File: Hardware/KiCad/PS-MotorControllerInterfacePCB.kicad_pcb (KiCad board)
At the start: 2 copper layers, 59.1 x 75.7 mm, 118 parts, among them IC1 LM74502HDDFR, IC2 LM74502HDDFR, J1 CAN board out, J2 PWR board, J3 CAN board in, J4 53307-2471, J5 PWR Moco, J6 Candapter, J7 CAN board -> mppt +moco, J8 CAN mppts + moco -> board, J9 Conn_01x06, Q1 IRLML0030, Q2 IRLML0030, Q3 NVMFWS1D7N04XMT1G, Q4 NVMFWS1D7N04XMT1G, Q5 771-BUK6M61-60PX, Q6 NVMFWS1D7N04XMT1G, Q7 NVMFWS1D7N04XMT1G, U1 LMR33630ADDA

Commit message: revb
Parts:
- moved 12V1 6.72 mm to (198.9, 70.3), turned to 0 degrees
- moved R3 5.44 mm to (198.9, 68.4), turned to 0 degrees
- moved Q1 5.19 mm to (194.3, 96.3)
- moved R_PD1 5.19 mm to (194.4, 93.5)
- moved R_G1 5.18 mm to (194.4, 91.9)
- moved TP6 5.16 mm to (190.4, 96.1)
- moved LED6 5.15 mm to (190.4, 94.2), turned to 0 degrees
- moved R25 5.15 mm to (190.4, 92.6), turned to 180 degrees
- moved TP7 3.76 mm to (185.2, 96.1)
- moved LED7 3.74 mm to (185.2, 94.2), turned to 0 degrees
- moved R26 3.74 mm to (185.2, 92.7), turned to 180 degrees
- moved LVPWR2 3.33 mm to (198.9, 66.8), turned to 180 degrees
- moved LED5 2.47 mm to (179.9, 94.2)
- moved R24 2.47 mm to (179.9, 92.7)
- moved TP5 2.42 mm to (180.0, 96.1)
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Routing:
- net GND: track 28.6 -> 44.1 mm, vias 8 -> 12
- net /PWM_FAN_A: track 55.2 -> 59.9 mm
- net /Fans/FAN_B_NEG: track 15.4 -> 19.2 mm
- net /LED4: track 13.9 -> 17.6 mm
- net /LED5: track 11.3 -> 13.6 mm
- net /LED3: track 7.47 -> 9.74 mm
- net /PWM_FAN_B: track 36.9 -> 38.9 mm
- net /FANS_IN: track 59.8 -> 61.2 mm
- net /LED1: track 11.8 -> 13.1 mm
- net /CAN_H: track 154.5 -> 155.6 mm
- net /CAN_L: track 145.2 -> 146.3 mm
- net Net-(LVPWR2-A): track 2.47 -> 1.66 mm
- net +24V: track 19.8 -> 20.5 mm
- net /LED2: track 8.11 -> 8.67 mm
- net /FAN_B_TACHO: track 34.1 -> 34.7 mm

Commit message: cleanup
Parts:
- moved LVPWR2 0.74 mm to (198.8, 67.5)
- moved R3 0.69 mm to (198.8, 69.1)
- moved 12V1 0.61 mm to (198.8, 70.9)
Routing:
- net GND: track 44.1 -> 44.5 mm, vias 12 -> 234
- added copper zone on B.Cu, net /12V_BUS
- added copper zone on B.Cu, net /VIN_24V

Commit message: sch changes, pre pcb changes
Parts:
- J1, J3: footprint Connector_Molex:Molex_Nano-Fit_105314-xx06_2x03_P2.50mm_Horizontal -> UTSVT_Connectors:105314-1306
- J2, J5, J6: footprint Connector_Molex:Molex_Nano-Fit_105313-xx02_1x02_P2.50mm_Horizontal -> UTSVT_Connectors:105313-2102
- J7, J8: footprint Connector_Molex:Molex_Nano-Fit_105313-xx03_1x03_P2.50mm_Horizontal -> UTSVT_Connectors:105313-1103
- J9: footprint Connector_Molex:Molex_Nano-Fit_105313-xx06_1x06_P2.50mm_Horizontal -> UTSVT_Connectors:105313-1106
- moved H3 57.8 mm to (157.8, 92.5)
- moved J7 10.3 mm to (202.5, 59.5), turned to 0 degrees
- moved J8 10.1 mm to (205.2, 47.9), turned to 90 degrees
- moved J2 9.24 mm to (198.1, 47.9), turned to 90 degrees
- moved J5 7.51 mm to (202.6, 70.3), turned to 0 degrees
- moved 3V1 6.02 mm to (155.1, 87.6)
- moved LVPWR3 6.02 mm to (155.0, 84.2)
- moved R5 6.02 mm to (155.0, 85.7)
- moved C2 2.81 mm to (178.7, 61.2), turned to -90 degrees
- moved R15 1.68 mm to (182.3, 86.0)
- moved Z3 1.46 mm to (182.8, 61.3)
- moved 12V1 1.18 mm to (198.0, 71.8)
- moved LVPWR2 1.15 mm to (197.9, 68.3)
- moved R3 1.11 mm to (198.0, 69.8)
- moved J4 0.99 mm to (176.4, 86.1)
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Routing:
- net GND: track 44.5 -> 33.8 mm, vias 234 -> 219
- net Net-(U1-SW): track 8.25 -> 0.00 mm
- net +3V3: track 38.4 -> 46.3 mm
- net /CAN_H: track 155.6 -> 152.9 mm
- net /PWM_FAN_B: track 38.9 -> 36.4 mm
- net /RPP_EN12: track 17.3 -> 15.6 mm
- net /CAN_L: track 146.3 -> 147.8 mm
- net /FAN_B_TACHO: track 34.7 -> 33.6 mm
- net /LED3: track 9.74 -> 8.82 mm
- net /MESSAGE: track 28.9 -> 29.5 mm
- net /D_C: track 34.3 -> 34.9 mm
- net /S_OC: track 25.5 -> 26.1 mm
- net /M_FAULT: track 40.3 -> 40.8 mm
- added copper zone on F.Cu, net Net-(U1-SW)

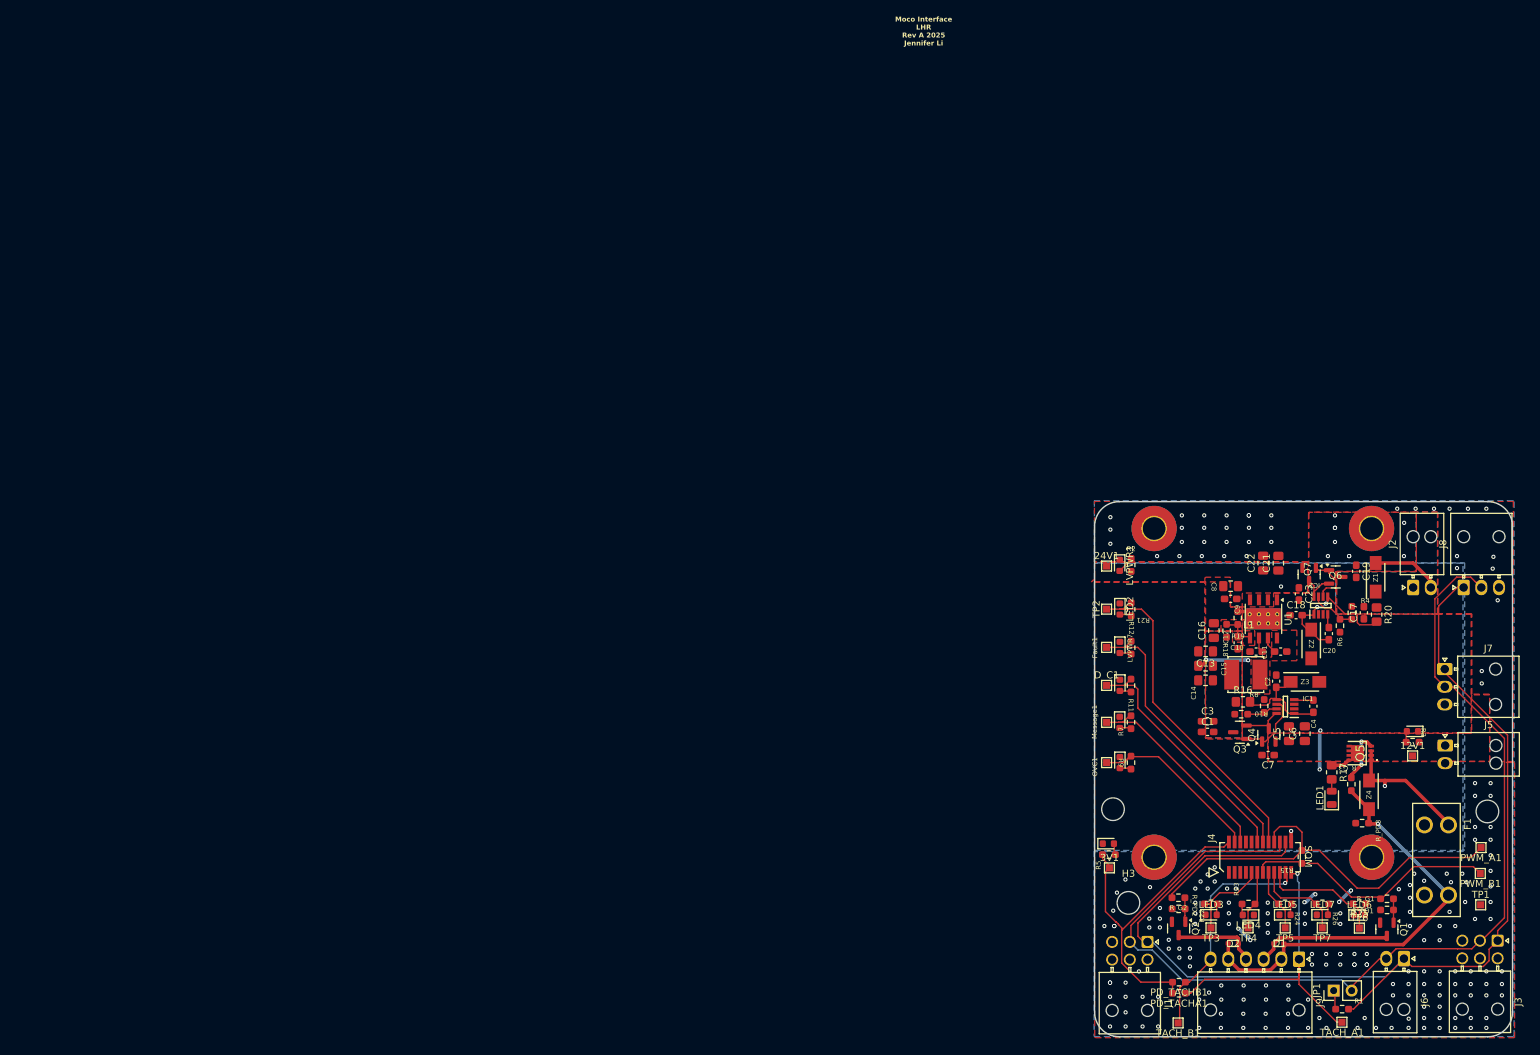
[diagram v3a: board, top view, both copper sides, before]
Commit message: layout ready for review
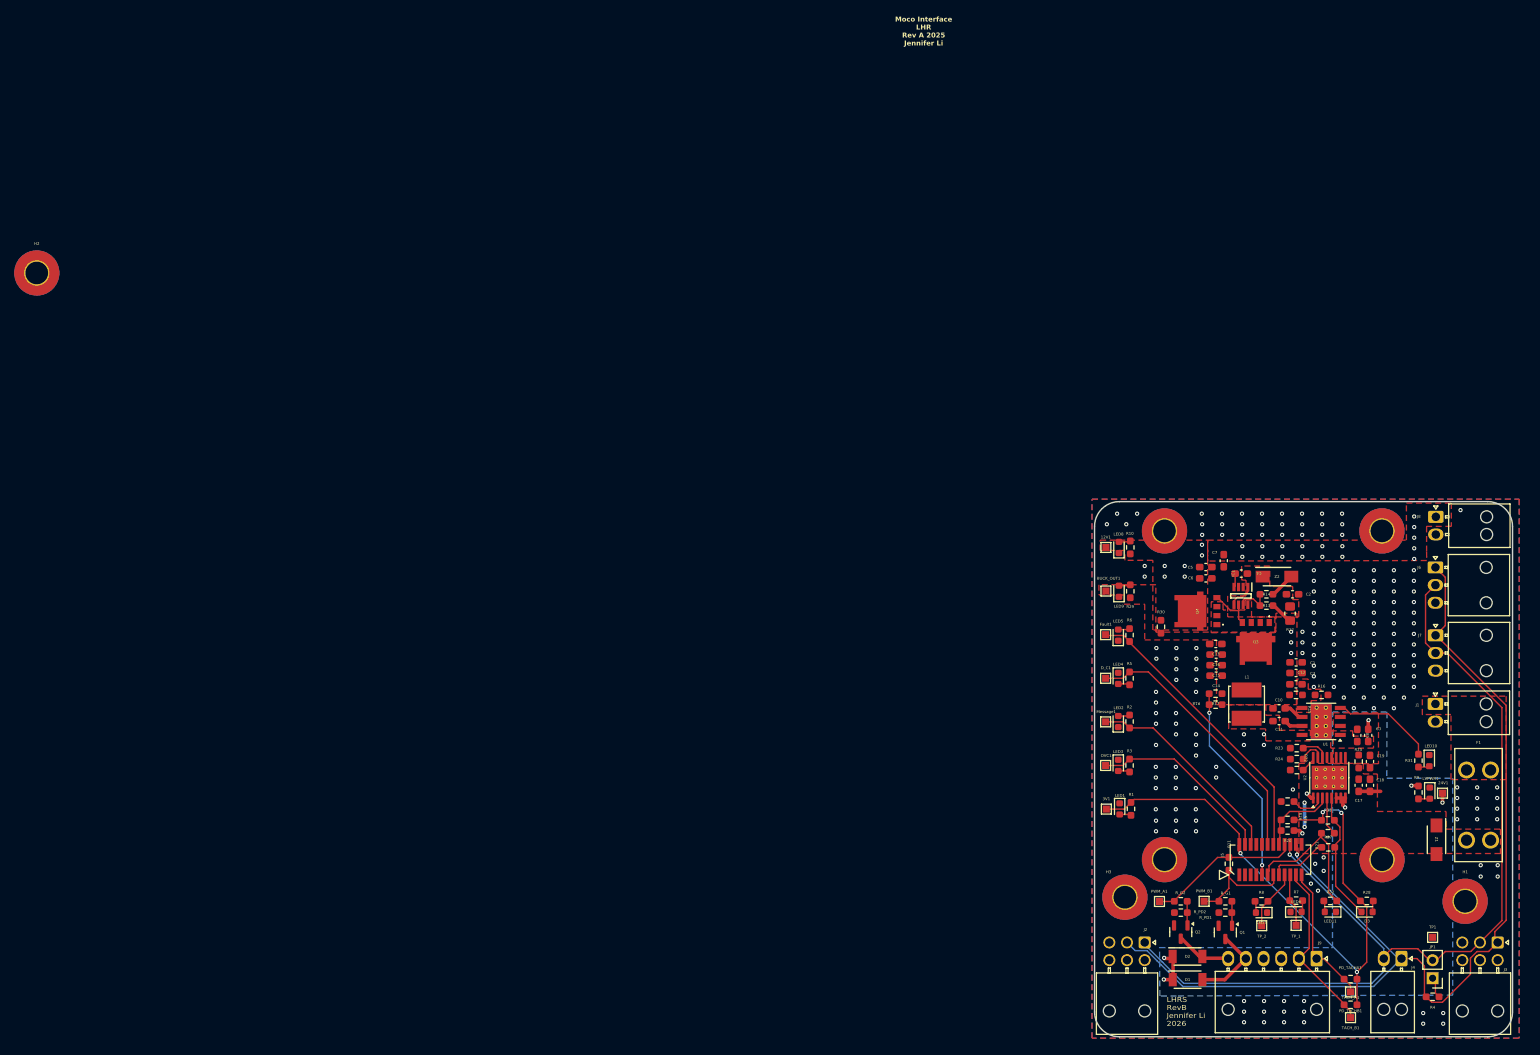
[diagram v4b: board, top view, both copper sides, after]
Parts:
- removed C20: 220n, Capacitor_SMD:C_0603_1608Metric_Pad1.08x0.95mm_HandSolder
- removed C21, C22: 10u, Capacitor_SMD:C_0805_2012Metric_Pad1.18x1.45mm_HandSolder
- removed C23: 0.1u, Capacitor_SMD:C_0603_1608Metric_Pad1.08x0.95mm_HandSolder
- removed IC2: LM74502HDDFR, UTSVT_Power:SOT65P280X110-8N
- removed LVPWR2, LVPWR3, LVPWR4, LVPWR5, LVPWR6, LVPWR7: LED, LED_SMD:LED_0603_1608Metric
- removed Q5: 771-BUK6M61-60PX, Moco:BUK9M34100EX
- removed Q6, Q7: NVMFWS1D7N04XMT1G, Package_TO_SOT_SMD:SOT-23
- removed R_G3: 100, Resistor_SMD:R_0603_1608Metric_Pad0.98x0.95mm_HandSolder
- removed R_PD3: 10k, Resistor_SMD:R_0603_1608Metric_Pad0.98x0.95mm_HandSolder
- removed TP2: LED, TestPoint:TestPoint_Pad_1.0x1.0mm
- removed TP3: LED1, TestPoint:TestPoint_Pad_1.0x1.0mm
- removed TP4: LED2, TestPoint:TestPoint_Pad_1.0x1.0mm
- removed TP5: LED3, TestPoint:TestPoint_Pad_1.0x1.0mm
- removed TP6: LED4, TestPoint:TestPoint_Pad_1.0x1.0mm
- removed TP7: LED5, TestPoint:TestPoint_Pad_1.0x1.0mm
- removed Z3: SMAF4758A, UTSVT_Passives:SODFL5026X125N
- removed Z4: SMAF4742A, UTSVT_Passives:SODFL5026X125N
- added BUCK_OUT1: TP_12V, TestPoint:TestPoint_Pad_1.0x1.0mm, F.Cu at (154.6, 48.4)
- added D3: LED_Small, LED_SMD:LED_0603_1608Metric, F.Cu at (191.5, 93.8)
- added LED10: LED, LED_SMD:LED_0603_1608Metric, F.Cu at (200.3, 72.4)
- added LED11: LED, LED_SMD:LED_0603_1608Metric, F.Cu at (186.3, 93.8)
- added LED8: LED, LED_SMD:LED_0603_1608Metric, F.Cu at (156.5, 42.3)
- added LED9: LED, LED_SMD:LED_0603_1608Metric, F.Cu at (156.5, 48.5)
- added R13: 100k, Resistor_SMD:R_0603_1608Metric_Pad0.98x0.95mm_HandSolder, F.Cu at (177.3, 50.5)
- added R14: 9。5k, Resistor_SMD:R_0603_1608Metric_Pad0.98x0.95mm_HandSolder, F.Cu at (177.3, 48.9)
- added R27: 10k, Resistor_SMD:R_0603_1608Metric_Pad0.98x0.95mm_HandSolder, F.Cu at (186.1, 84.7)
- added R28: 1k, Resistor_SMD:R_0603_1608Metric_Pad0.98x0.95mm_HandSolder, F.Cu at (191.5, 92.2)
- added R29: 4.3k, Resistor_SMD:R_0603_1608Metric_Pad0.98x0.95mm_HandSolder, F.Cu at (158.1, 48.5)
- added R30: 0, Resistor_SMD:R_0603_1608Metric_Pad0.98x0.95mm_HandSolder, F.Cu at (162.4, 53.5)
- added R31: 4.3k, Resistor_SMD:R_0603_1608Metric_Pad0.98x0.95mm_HandSolder, F.Cu at (198.8, 72.4)
- added R32: 1k, Resistor_SMD:R_0603_1608Metric_Pad0.98x0.95mm_HandSolder, F.Cu at (186.3, 92.2)
- added R33: 10k, Resistor_SMD:R_0603_1608Metric_Pad0.98x0.95mm_HandSolder, F.Cu at (186.0, 80.8)
- added TP_1: LED1, TestPoint:TestPoint_Pad_1.0x1.0mm, F.Cu at (181.5, 95.7)
- added TP_2: LED2, TestPoint:TestPoint_Pad_1.0x1.0mm, F.Cu at (176.6, 95.8)
- added U2: TPS27SA08-Q1, Package_SO:HTSSOP-16-1EP_4.4x5mm_P0.65mm_EP3.4x5mm_Mask2.66x2.46mm_ThermalVias, F.Cu at (186.2, 74.8)
- C13, C14, C15, C16, C5, C6, C8: footprint Capacitor_SMD:C_0805_2012Metric_Pad1.18x1.45mm_HandSolder -> Capacitor_SMD:C_0603_1608Metric_Pad1.08x0.95mm_HandSolder
- C17: value .1u -> 1u
- C18: value 1u -> 10u
- C19: value .1u -> 22n
- D1, D2: footprint easyeda2kicad:SOD-523F_L1.2-W0.8-LS1.7-RD -> UTSVT_Passives:SODFL4724X108N
- D_C1: value TP_D_C -> TP_DC
- H1, H2, H3: footprint MountingHole:MountingHole_3.2mm_M3 -> MountingHole:MountingHole_3.2mm_M3_Pad_TopBottom
- J1: value CAN board out -> PWR board; footprint UTSVT_Connectors:105314-1306 -> UTSVT_Connectors:105313-2102
- J2: value PWR board -> CAN board out; footprint UTSVT_Connectors:105313-2102 -> UTSVT_Connectors:105314-1306
- J4: value 53307-2471 -> Candapter; footprint UTSVT_Connectors:PeripheralSOM -> UTSVT_Connectors:105313-2102
- J5: value PWR Moco -> 53307-2471; footprint UTSVT_Connectors:105313-2102 -> UTSVT_Connectors:PeripheralSOM
- J6: value Candapter -> CAN board -> mppt +moco; footprint UTSVT_Connectors:105313-2102 -> UTSVT_Connectors:105313-1103
- J7: value CAN board -> mppt +moco -> CAN mppts + moco -> board
- J8: value CAN mppts + moco -> board -> PWR Moco; footprint UTSVT_Connectors:105313-1103 -> UTSVT_Connectors:105313-2102
- LED1: value 20mA -> LED; footprint LED_SMD:LED_0805_2012Metric -> LED_SMD:LED_0603_1608Metric
- Q3, Q4: footprint Package_TO_SOT_SMD:SOT-23 -> UTSVT_Power:NVMFWS3D0P04M8LT1G
- R1: value 120 -> 1k
- R10: value 100k -> 4.3k
- R11, R25: value 4.3k -> 0
- R12: value 4.3k -> 10k; footprint Resistor_SMD:R_0603_1608Metric_Pad0.98x0.95mm_HandSolder -> Resistor_SMD:R_0805_2012Metric_Pad1.20x1.40mm_HandSolder
- R15: value 0 -> 100k
- R16: value 10k -> 9.09k; footprint Resistor_SMD:R_0805_2012Metric_Pad1.20x1.40mm_HandSolder -> Resistor_SMD:R_0603_1608Metric_Pad0.98x0.95mm_HandSolder
- R17: value 4.3k -> 100k; footprint Resistor_SMD:R_0805_2012Metric_Pad1.20x1.40mm_HandSolder -> Resistor_SMD:R_0603_1608Metric_Pad0.98x0.95mm_HandSolder
- R18: value 100k -> 9.09k
- R19: value 9.09k -> 1k
- R2, R26, R3, R5, R7: value 4.3k -> 1k
- R20: value 10k -> 1k; footprint Resistor_SMD:R_0805_2012Metric_Pad1.20x1.40mm_HandSolder -> Resistor_SMD:R_0603_1608Metric_Pad0.98x0.95mm_HandSolder
- R21, R22, R23, R24: value 4.3k -> 10k
- R4: value 200k -> 120
- R6: value 9k -> 1k
- R8: value 9。5k -> 1k
- R_G1, R_G2: value 100 -> 1k
- moved H2 170.0 mm to (3.48, 3.48)
- moved J2 62.9 mm to (160.1, 98.1), turned to -90 degrees
- moved 24V1 57.3 mm to (202.2, 77.0)
- moved J6 55.5 mm to (201.2, 45.1), turned to 0 degrees
- moved R4 55.5 mm to (200.8, 105.8), turned to 0 degrees
- moved LVPWR1 54.4 mm to (200.4, 77.0)
- moved J1 52.8 mm to (201.2, 64.4), turned to 0 degrees
- moved 12V1 52.4 mm to (154.6, 42.3)
- moved PWM_A1 46.1 mm to (162.2, 92.3)
- moved LED5 46.0 mm to (156.4, 54.7), turned to 90 degrees
- moved R21 42.1 mm to (186.0, 82.7), turned to 0 degrees
- moved R1 41.1 mm to (158.2, 79.2), turned to 90 degrees
- moved R9 40.9 mm to (198.8, 76.9)
- moved R3 40.1 mm to (158.0, 73.1), turned to 90 degrees
- moved PWM_B1 39.2 mm to (168.5, 92.3)
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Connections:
- C17 pad 1: GND -> /PSOM_PWR
- C17 pad 2: /VIN_24V -> GND
- C18 pad 1: GND -> /PSOM_PWR
- C18 pad 2: /RPP_EN24 -> GND
- C19 pad 1: GND -> +24V
- C19 pad 2: /VIN_24V -> GND
- C2 pad 2: /RPP_EN12 -> /Power12V/RPP_EN
- C4 pad 1: /RPP_EN12 -> /Power12V/RPP_EN
- D1 pad 1: /FANS_IN -> +24V
- D2 pad 1: /FANS_IN -> +24V
- F1 pad 1: +24V -> /VIN_24V
- F1 pad 2: /FANS_IN -> /PSOM_PWR
- IC1 pad 1: /RPP_EN12 -> /Power12V/RPP_EN
- IC1 pad 5: /RPP_EN12 -> /Power12V/RPP_EN
- IC1 pad 6: Net-(IC1-GATE) -> /Power12V/Gate
- IC1 pad 7: /Power12V/OV -> Net-(IC1-OV)
- IC1 pad 8: Net-(IC1-SRC) -> /Power12V/Src
- J1 pad 1: /CAN_H -> /VIN_24V
- J1 pad 2: /CAN_L -> GND
- J2 pad 1: /VIN_24V -> /CAN_L
- J2 pad 2: GND -> /CAN_H
- J4 pad 1: GND -> /CAN_H
- J4 pad 2: +3V3 -> /CAN_L
- J5 pad 1: +12V -> GND
- J5 pad 2: GND -> +3V3
- J8 pad 1: /CAN_H -> +12V
- J8 pad 2: /CAN_L -> GND
- J9 pad 2: /FANS_IN -> /FAN_B_TACHO
- J9 pad 3: /Fans/FAN_B_NEG -> +24V
- J9 pad 4: /Fans/FAN_A_NEG -> +24V
- J9 pad 5: /FANS_IN -> /Fans/FAN_B_NEG
- J9 pad 6: /FAN_B_TACHO -> /Fans/FAN_A_NEG
- Q3 pad 1: Net-(IC1-GATE) -> /Power12V/Src
- Q3 pad 2: Net-(IC1-SRC) -> /Power12V/Src
- Q3 pad 3: /12V_BUS -> /Power12V/Src
- Q4 pad 1: Net-(IC1-GATE) -> /Power12V/Src
- Q4 pad 2: +12V -> /Power12V/Src
- Q4 pad 3: Net-(IC1-SRC) -> /Power12V/Src
- R1 pad 1: /CAN_H -> Net-(LED1-A)
- R1 pad 2: Net-(JP1-A) -> +3V3
- R10 pad 1: /Power12V/OV -> Net-(LED8-A)
- R10 pad 2: /12V_BUS -> +12V
- R11 pad 1: Net-(LVPWR6-A) -> /PWM_FAN_A
- R11 pad 2: /D_C -> /PWM_FAN_B
- R12 pad 1: Net-(LVPWR7-A) -> /12V_BUS
- R12 pad 2: /M_FAULT -> /Power12V/RPP_EN
- R15 pad 1: /PWM_FAN_A -> /12V_BUS
- R15 pad 2: /PWM_FAN_B -> Net-(U1-FB)
- R16 pad 1: /12V_BUS -> Net-(U1-FB)
- R16 pad 2: /RPP_EN12 -> GND
- R17 pad 1: Net-(Q5-D_1) -> /12V_BUS
- R17 pad 2: Net-(LED1-A) -> /12V_SENSE
- R18 pad 1: /12V_BUS -> /12V_SENSE
- R18 pad 2: Net-(U1-FB) -> GND
- R19 pad 1: Net-(U1-FB) -> +3V3
- R19 pad 2: GND -> /LATCH
- R2 pad 1: Net-(LVPWR1-A) -> Net-(LED2-A)
- R2 pad 2: +24V -> /MESSAGE
- R20 pad 1: /VIN_24V -> GND
- R20 pad 2: /RPP_EN24 -> /LATCH
- R21 pad 1: Net-(LED2-A) -> /EN
- R21 pad 2: /LED -> Net-(U2-EN)
- R22 pad 1: Net-(LED3-A) -> GND
- R22 pad 2: /LED1 -> Net-(U2-DIA_EN)
- R23 pad 1: Net-(LED4-A) -> GND
- R23 pad 2: /LED2 -> Net-(U2-SEL1)
- R24 pad 1: Net-(LED5-A) -> GND
- R24 pad 2: /LED3 -> Net-(U2-SEL2)
- R25 pad 1: Net-(LED6-A) -> /PSOM_PWR
- R25 pad 2: /LED4 -> +24V
- R26 pad 1: Net-(LED7-A) -> Net-(U2-SNS)
- R26 pad 2: /LED5 -> GND
- R3 pad 1: Net-(LVPWR2-A) -> Net-(LED3-A)
- R3 pad 2: +12V -> /S_OC
- R4 pad 1: /Power24V/OV -> /CAN_H
- R4 pad 2: /VIN_24V -> Net-(JP1-A)
- R5 pad 1: Net-(LVPWR3-A) -> Net-(LED4-A)
- R5 pad 2: +3V3 -> /D_C
- R6 pad 1: GND -> Net-(LED5-A)
- R6 pad 2: /Power24V/OV -> /M_FAULT
- R7 pad 1: Net-(LVPWR4-A) -> Net-(LED6-A)
- R7 pad 2: /MESSAGE -> /LED1
- R8 pad 1: /Power12V/OV -> Net-(LED7-A)
- R8 pad 2: GND -> /LED2
- R9 pad 1: Net-(LVPWR5-A) -> Net-(LVPWR1-A)
- R9 pad 2: /S_OC -> +24V
- U1 pad 4: unconnected-(U1-PG-Pad4) -> Net-(U1-PG)
- Z1 pad 1: /VIN_24V -> /PSOM_PWR
- Z2 pad 1: /RPP_EN24 -> /Power12V/RPP_EN
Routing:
- net /FANS_IN: track 61.2 -> 0.00 mm, vias 1 -> 0
- net /LED: track 47.3 -> 0.00 mm
- net +3V3: track 46.3 -> 84.8 mm, vias 0 -> 4
- net /PWM_FAN_A: track 60.0 -> 22.1 mm
- net /12V_SENSE: track 0.00 -> 28.7 mm, vias 0 -> 2
- net GND: track 33.8 -> 9.26 mm, vias 219 -> 223
- net /FAN_A_TACHO: track 44.7 -> 20.4 mm, vias 1 -> 0
- net /EN: track 0.00 -> 21.0 mm
- net /RPP_EN24: track 20.9 -> 0.00 mm, vias 2 -> 0
- net /PWM_FAN_B: track 36.4 -> 16.1 mm
- net Net-(D3-K): track 0.00 -> 18.5 mm
- net /LED4: track 17.2 -> 0.00 mm
- net /RPP_EN12: track 15.6 -> 0.00 mm
- net Net-(U1-PG): track 0.00 -> 14.6 mm
- net /CAN_L: track 147.8 -> 134.4 mm, vias 0 -> 1
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- added copper zone on F.Cu, net /PSOM_PWR
- added copper zone on F.Cu, net /Power12V/RPP_EN
- added copper zone on F.Cu, net /Power12V/Src
- removed copper zone on B.Cu, net /12V_BUS
- removed copper zone on B.Cu, net /VIN_24V
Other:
- board text added: "LHRS RevB Jennifer Li 2026"
